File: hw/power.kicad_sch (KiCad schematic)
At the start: 20 parts, among them J4 Prog/debug, Q4 AO3401A, Q5 8205A, U2 TP4057, U3 AP7361C-25ER-13, U4 DW01A

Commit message: WIP
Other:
- note added: "TODO: LED backlight needs 2.9--3.1 V -- and 20 mA exactly -> make a current generator?"
- note removed: "TODO: LED backlight needs 2.9--3.1 V -- and 20 mA exactly"
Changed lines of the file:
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@@
 		)
 	)
-	(text "TODO: LED backlight needs 2.9--3.1 V -- and 20 mA exactly"
+	(text "TODO: LED backlight needs 2.9--3.1 V -- and 20 mA exactly -> make a current generator?"
 		(exclude_from_sim no)
 		(at 175.514 68.58 0)

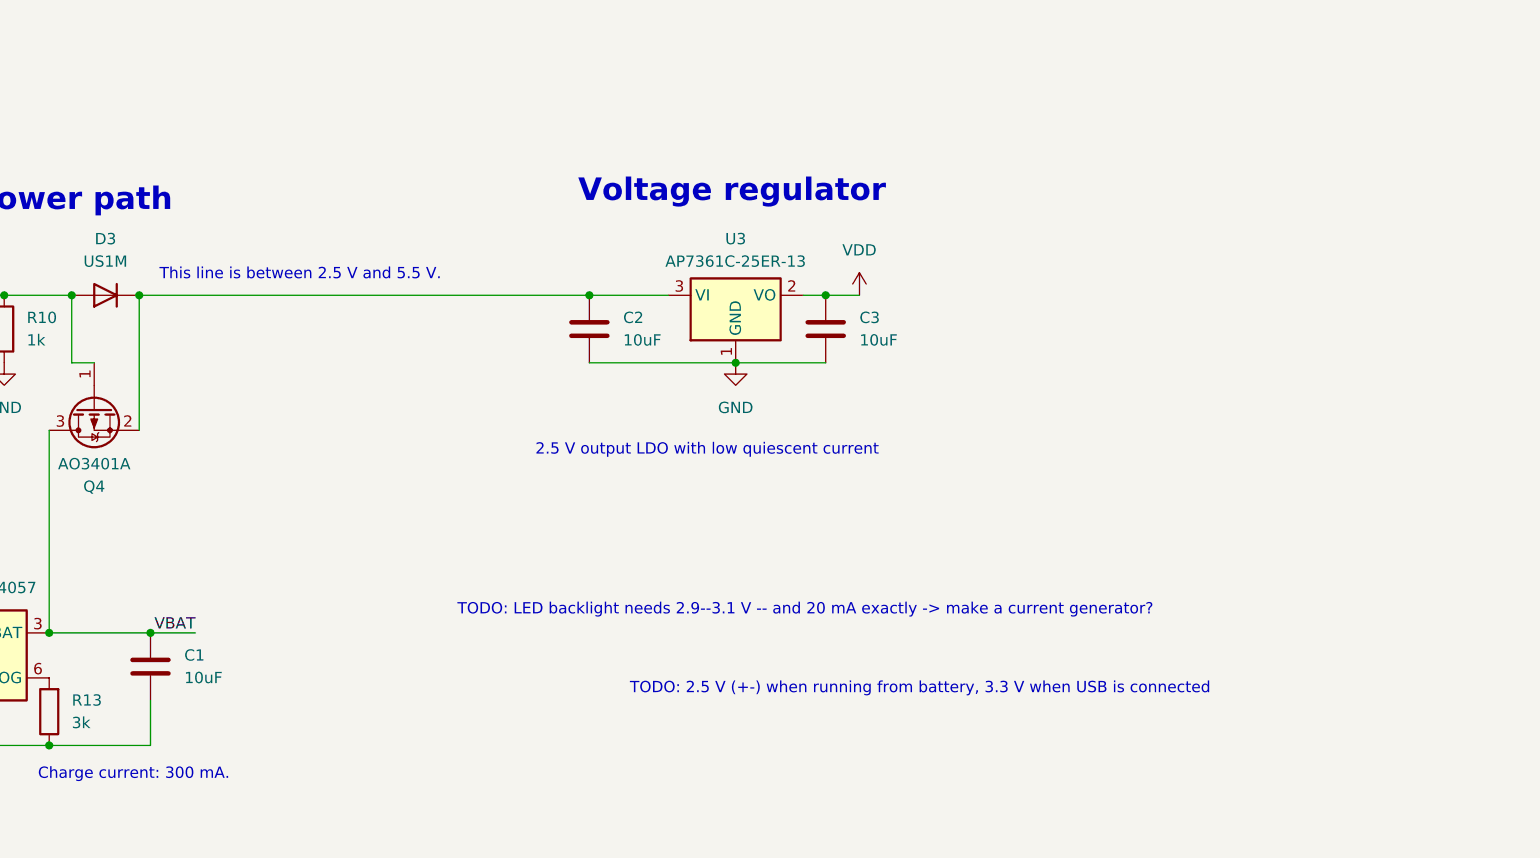
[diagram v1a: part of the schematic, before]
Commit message: Added different voltage regulator.
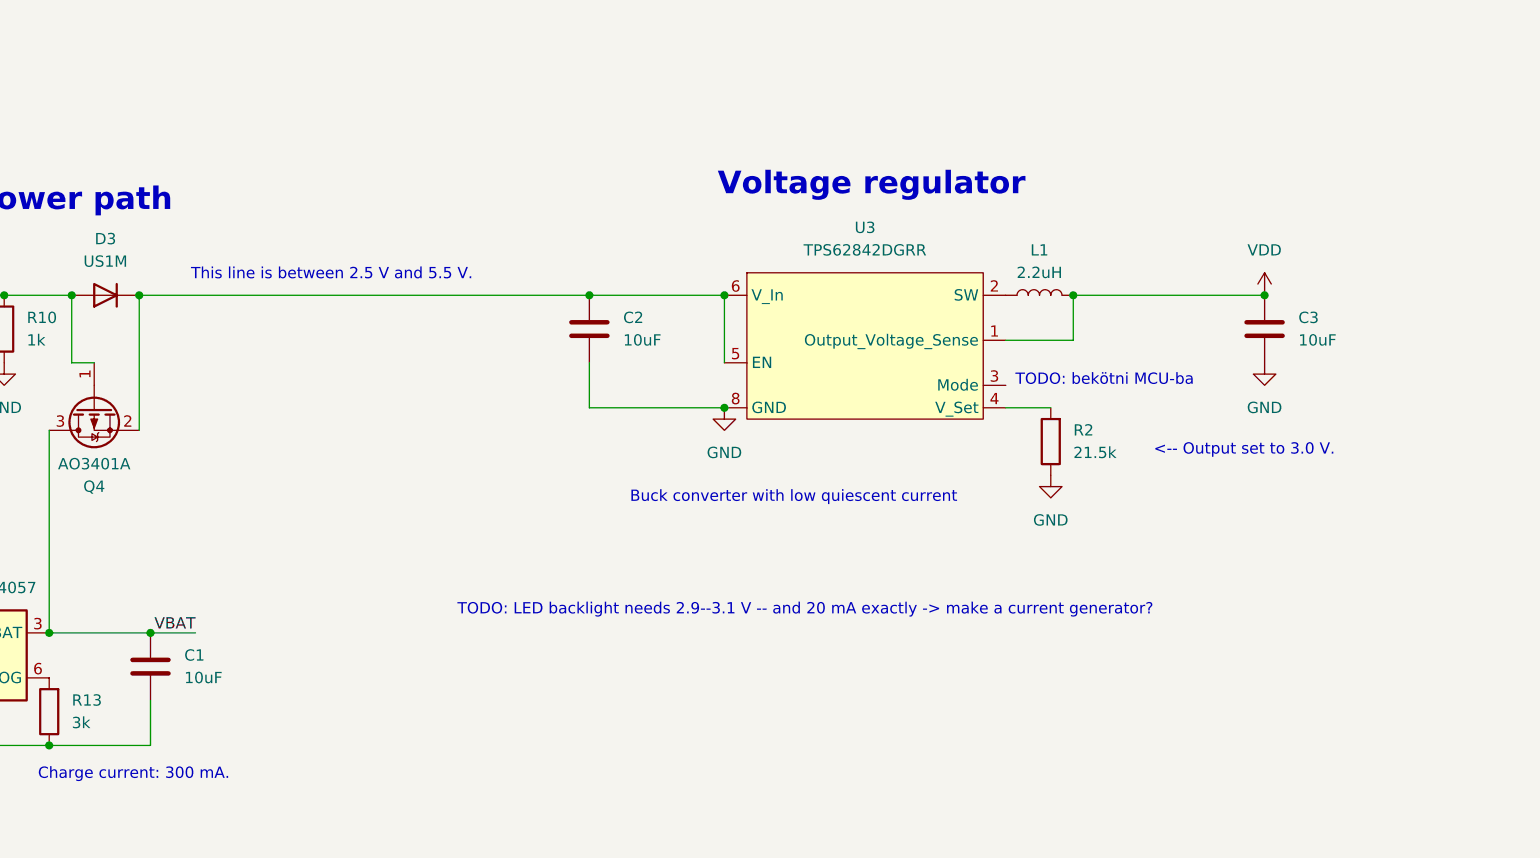
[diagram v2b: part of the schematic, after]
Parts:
- removed U3: AP7361C-25ER-13, Package_TO_SOT_SMD:SOT-223-3_TabPin2, symbol Regulator_Linear:AMS1117-2.5
- added L1: 2.2uH, symbol Device:L
- added R2: 21.5k, Resistor_SMD:R_0805_2012Metric, symbol Device:R
- added U3: TPS62842DGRR, Package_SO:HVSSOP-8-1EP_3x3mm_P0.65mm_EP1.57x1.89mm, symbol sem18:TPS62842DGRR
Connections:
- net GND: now also R2.1, U3.8 (GND), U3.9 (GND)
- net VDD: now also L1.2, U3.1 (Output_Voltage_Sense)
- net at C2.1, D3.1 (K), Q4.2 (S): now also U3.5 (EN), U3.6 (V_In)
- new net: R2.2, U3.4 (V_Set)
- new net: L1.1, U3.2 (SW)
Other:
- note added: "<-- Output set to 3.0 V."
- note added: "Buck converter with low quiescent current"
- note added: "TODO: bekötni MCU-ba"
- note removed: "2.5 V output LDO with low quiescent current"
- note removed: "TODO: 2.5 V (+-) when running from battery, 3.3 V when USB is connected"
- moved on the sheet: C3

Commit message: WIP
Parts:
- added R4: 100k, Resistor_SMD:R_0805_2012Metric, symbol Device:R
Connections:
- net GND: now also R4.1
- net at U3.3 (Mode): now also R4.2
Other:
- note added: "^^ Output set to 3.0 V."
- note removed: "<-- Output set to 3.0 V."
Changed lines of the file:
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@@
 		)
 	)
-	(text "<-- Output set to 3.0 V."
+	(text "^^ Output set to 3.0 V."
 		(exclude_from_sim no)
-		(at 225.044 50.546 0)
+		(at 212.852 62.738 0)
 		(effects
 			(font
@@
 	)
 	(junction
+		(at 203.2 53.34)
+		(diameter 0)
+		(color 0 0 0 0)
+	)
+	(junction
 		(at 87.63 140.97)
 		(diameter 0)
@@
 	(wire
 		(pts
+			(xy 214.63 43.18) (xy 214.63 45.72)
+		)
+		(stroke
+			(width 0)
+			(type default)
+		)
+	)
+	(wire
+		(pts
 			(xy 100.33 33.02) (xy 100.33 48.26)
 		)
@@
 	(wire
 		(pts
+			(xy 198.12 43.18) (xy 214.63 43.18)
+		)
+		(stroke
+			(width 0)
+			(type default)
+		)
+	)
+	(wire
+		(pts
 			(xy 87.63 140.97) (xy 87.63 151.13)
 		)
@@
 		(pts
 			(xy 87.63 133.35) (xy 99.06 133.35)
+		)
+		(stroke
+			(width 0)
+			(type default)
+		)
+	)
+	(wire
+		(pts
+			(xy 203.2 53.34) (xy 214.63 53.34)
 		)
 		(stroke
@@
 					(unit 1)
 				)
+			)
+		)
+	)
+	(symbol
+		(lib_id "Device:R")
+		(at 214.63 49.53 180)
+		(unit 1)
+		(exclude_from_sim no)
+		(in_bom yes)
+		(on_board yes)
+		(dnp no)
+		(fields_autoplaced yes)
+		(property "Reference" "R4"
+			(at 217.17 48.2599 0)
+			(effects
+				(font
+					(size 1.27 1.27)
+				)
+				(justify right)
+			)
+		)
+		(property "Value" "100k"
+			(at 217.17 50.7999 0)
+			(effects
+				(font
+					(size 1.27 1.27)
+				)
+				(justify right)
+			)
+		)
+		(property "Footprint" "Resistor_SMD:R_0805_2012Metric"
+			(at 216.408 49.53 90)
+			(effects
+				(font
+					(size 1.27 1.27)
+				)
+				(hide yes)
+			)
+		)
+		(property "Datasheet" "~"
+			(at 214.63 49.53 0)
+			(effects
+				(font
+					(size 1.27 1.27)
+				)
+				(hide yes)
+			)
+		)
+		(property "Description" "Resistor"
+			(at 214.63 49.53 0)
+			(effects
+				(font
+					(size 1.27 1.27)
+				)
+				(hide yes)
+			)
+		)
+		(pin "2"
+		)
+		(pin "1"
+		)
+		(instances
+			(project "sem18"
+				(path "/d844aefd-19cf-4889-9465-41f3f1184bf3/0a7f8c5e-87fd-44f3-ac0d-848b1ec15823"
+					(reference "R4")
+					(unit 1)
+				)

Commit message: Schematic is finished. Needs some touch-ups and component selection (esp. for switches).
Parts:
- renumbered C8 to C1, C9 to C2, C2 to C3, C3 to C4, C1 to C5, C7 to C6, D3 to D1, D4 to D2, J4 to J2, Q4 to Q1, Q5 to Q2, R10 to R3, R2 to R4, R4 to R5, R12 to R6, R13 to R7, R16 to R8, R17 to R9, U3 to U2, U2 to U3
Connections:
- net +VSW: now reaches C3.1, D1.1 (K), Q1.2 (S), U2.5 (EN), U2.6 (V_In)
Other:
- note removed: "TODO: LED backlight needs 2.9--3.1 V -- and 20 mA exactly -> make a current generator?"
- note removed: "TODO: bekötni MCU-ba"
- moved on the sheet: BT1, C1, C2, C3, C4, C5, C6, D1, D2, L1, Q1, Q2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

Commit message: WIP
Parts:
- removed J2: Prog/debug, Connector_PinHeader_2.54mm:PinHeader_1x06_P2.54mm_Vertical, symbol Connector_Generic:Conn_01x06
- C2, C6: footprint Capacitor_SMD:C_0805_2012Metric -> Capacitor_SMD:C_0603_1608Metric
- D2: footprint LED_THT:LED_D3.0mm-3 -> LED_SMD:LED_LiteOn_LTST-S326
- L1: footprint (none) -> Inductor_SMD:L_APV_ANR3012
- R3, R4, R5, R6, R7, R8, R9: footprint Resistor_SMD:R_0805_2012Metric -> Resistor_SMD:R_0603_1608Metric
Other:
- note removed: "ARM Serial Wire Debug (SWD) interface"
- note removed: "Pinout compatible with integrated ST-Link on STM32 Nucleo boards. Watch out for the operating voltage (2.5V)!"
- note removed: "Programming/debug"

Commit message: Different microcontroller. Placed most of the components too.
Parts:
- removed BT1: Li-po, symbol Device:Battery_Cell
- removed D2: Status, LED_SMD:LED_LiteOn_LTST-S326, symbol Device:LED_Dual_KAK
- removed R6: 1k, Resistor_SMD:R_0603_1608Metric, symbol Device:R
- added TP1: Batt+, Connector_Wire:SolderWirePad_1x01_SMD_1x2mm, symbol Connector:TestPoint
- added TP2: Batt-, Connector_Wire:SolderWirePad_1x01_SMD_1x2mm, symbol Connector:TestPoint
- C1, C3, C4, C5: footprint Capacitor_SMD:C_1206_3216Metric -> Capacitor_SMD:C_0805_2012Metric
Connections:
- net VBAT: now also TP1.1
- net at C6.2, Q2.1 (D1), U4.6 (GND): now also TP2.1
- net Buck_Mode: now reaches R5.2, U2.3 (Mode)
- net CHARGER_nCharge: now reaches U3.1 (~{CHRG})
- net CHARGER_Standby: now reaches U3.5 (STDBY)
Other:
- moved on the sheet: C2
